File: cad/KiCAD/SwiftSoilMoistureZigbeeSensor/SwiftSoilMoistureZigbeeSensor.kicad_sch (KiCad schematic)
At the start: 12 parts, among them J1 Probe, J3 ARM SWD, Q1 BSS84, SW1 Factory Reset, U1 TPS61221DCK, U2 E73-2G4M08S1C

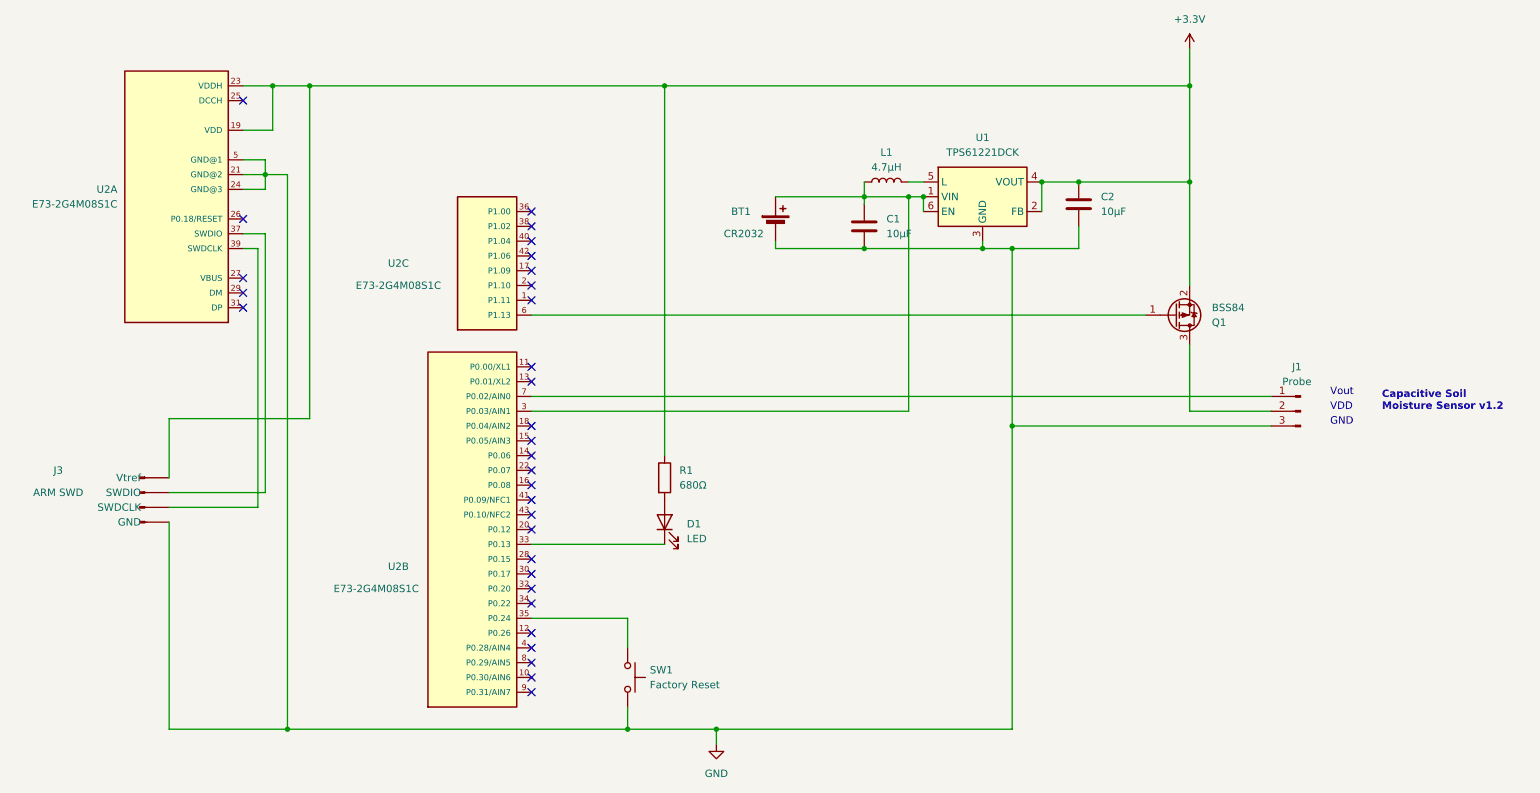
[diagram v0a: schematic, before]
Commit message: Changed TPS61221 to TPS61097
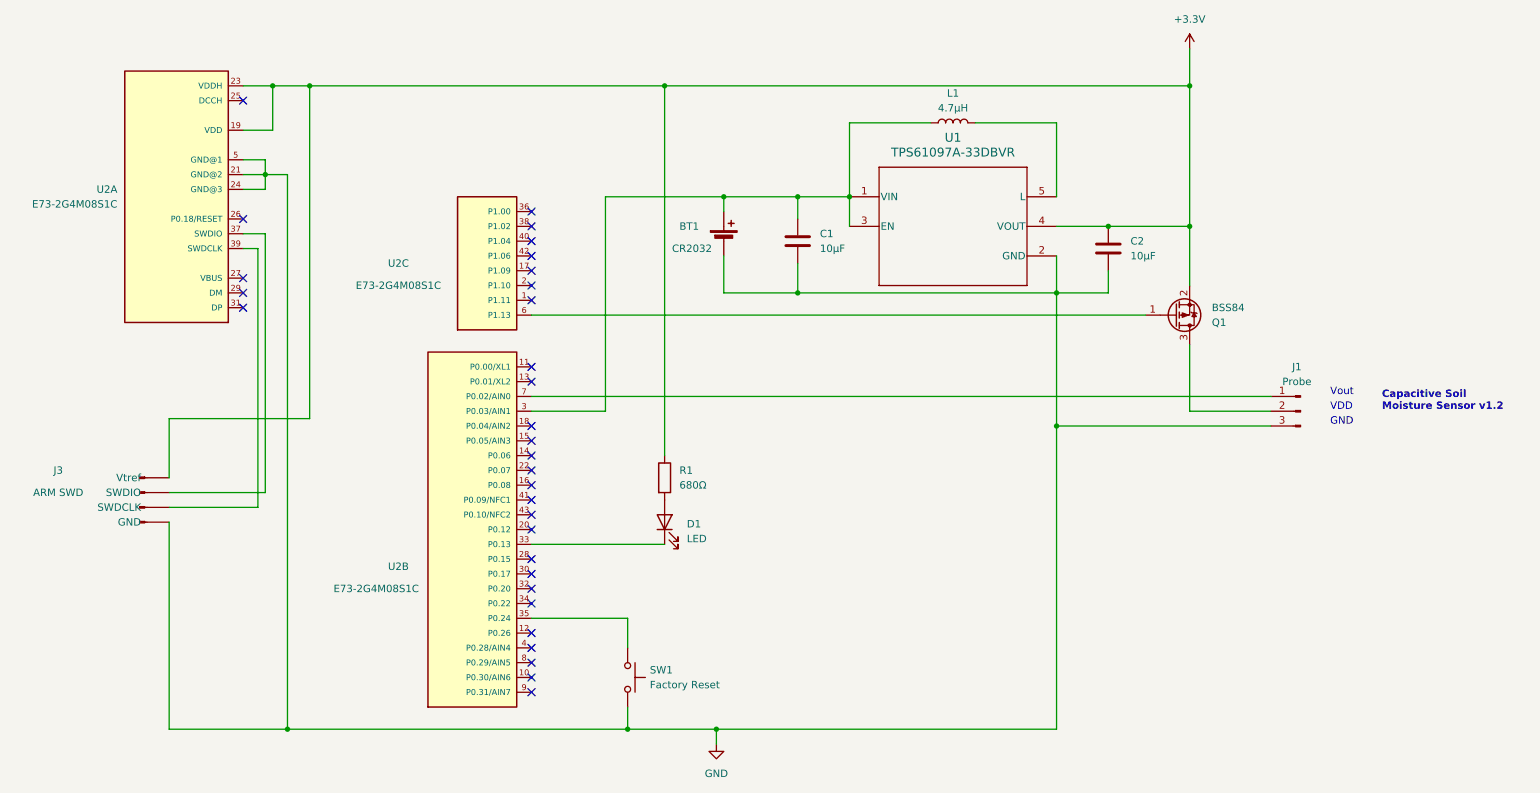
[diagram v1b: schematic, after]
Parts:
- removed U1: TPS61221DCK, Package_TO_SOT_SMD:Texas_R-PDSO-G6, symbol Regulator_Switching:TPS61221DCK
- added U1: TPS61097A-33DBVR, Package_TO_SOT_SMD:SOT-23-5_HandSoldering, symbol TPS61097A-33:TPS61097A-33DBVR
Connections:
- net +3.3V: now also U1.4 (VOUT)
- net GND: now also U1.2 (GND)
- net at BT1.1 (+), C1.1, L1.1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: now also U1.1 (VIN), U1.3 (EN)
- net at L1.2: now also U1.5 (L)
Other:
- moved on the sheet: BT1, C1, C2, L1

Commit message: BOM update
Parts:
- U1: LCSC (none) -> C2071172
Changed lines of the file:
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@@
       (effects (font (size 1.27 1.27) italic) hide)
+    )
+    (property "LCSC" "C2071172" (at 186.69 57.15 0)
+      (effects (font (size 1.27 1.27)) hide)
     )
     (pin "4")
